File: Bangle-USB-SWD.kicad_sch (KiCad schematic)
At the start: 3 parts, among them J1 USB_A, J2 Conn_02x05_Odd_Even, J3 Conn_01x02_Male

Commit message: add schematics PDF and top/bottom 3D previews
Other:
- company: (none) -> (c) Digitaluhr Manufaktur, Nicole Faerber
- title: (none) -> Bangle.JS2 SWD breakout
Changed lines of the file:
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@@
 (kicad_sch (version 20211123) (generator eeschema)
   (paper "A4")
+  (title_block
+    (title "Bangle.JS2 SWD breakout")
+    (date "2022-03-20")
+    (rev "V0.1")
+    (company "(c) Digitaluhr Manufaktur, Nicole Faerber")
+    (comment 1 "License: GPL V2.0")
+  )
   (wire (pts (xy 129.54 86.36) (xy 135.89 86.36))
     (stroke (width 0) (type default) (color 0 0 0 0))

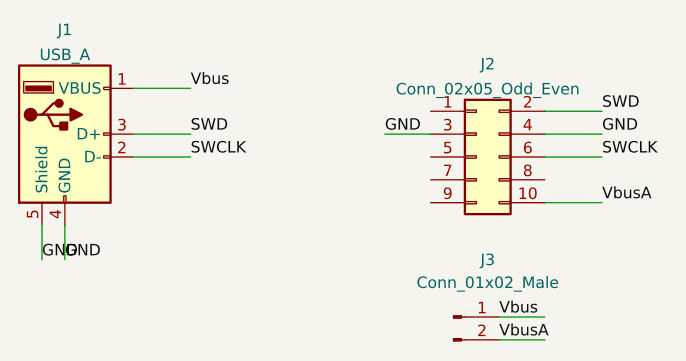
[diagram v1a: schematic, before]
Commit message: oops, SWDIO nd SWCLK swapped on USB type-A conntector, fixed
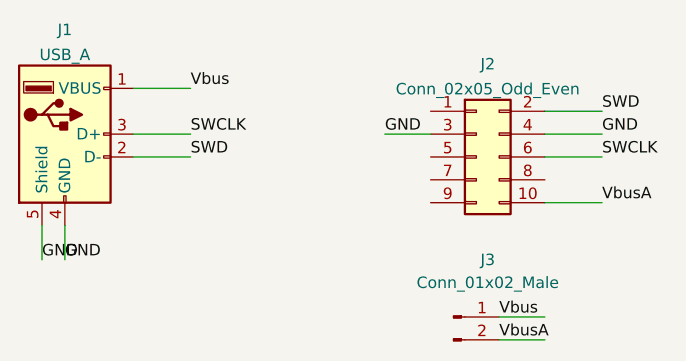
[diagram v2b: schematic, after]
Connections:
- net SWCLK: now also J1.3 (D+); no longer J1.2 (D-)
- net SWD: now also J1.2 (D-); no longer J1.3 (D+)
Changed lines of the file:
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@@
     (stroke (width 0) (type default) (color 0 0 0 0))
   )
-  (label "SWCLK" (at 90.17 81.28 0)
+  (label "SWD" (at 90.17 81.28 0)
     (effects (font (size 1.27 1.27)) (justify left bottom))
   )
@@
     (effects (font (size 1.27 1.27)) (justify left bottom))
   )
-  (label "SWD" (at 90.17 78.74 0)
+  (label "SWCLK" (at 90.17 78.74 0)
     (effects (font (size 1.27 1.27)) (justify left bottom))
   )
